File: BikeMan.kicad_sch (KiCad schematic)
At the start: 10 parts, among them J1 USB_A_stacked, J2 USB_A_stacked, J3 Conn_01x04_Female, J4 Barrel_Jack, J5 PushConnector_8pos, J6 PushConnector_8pos, J7 PushConnector_8pos

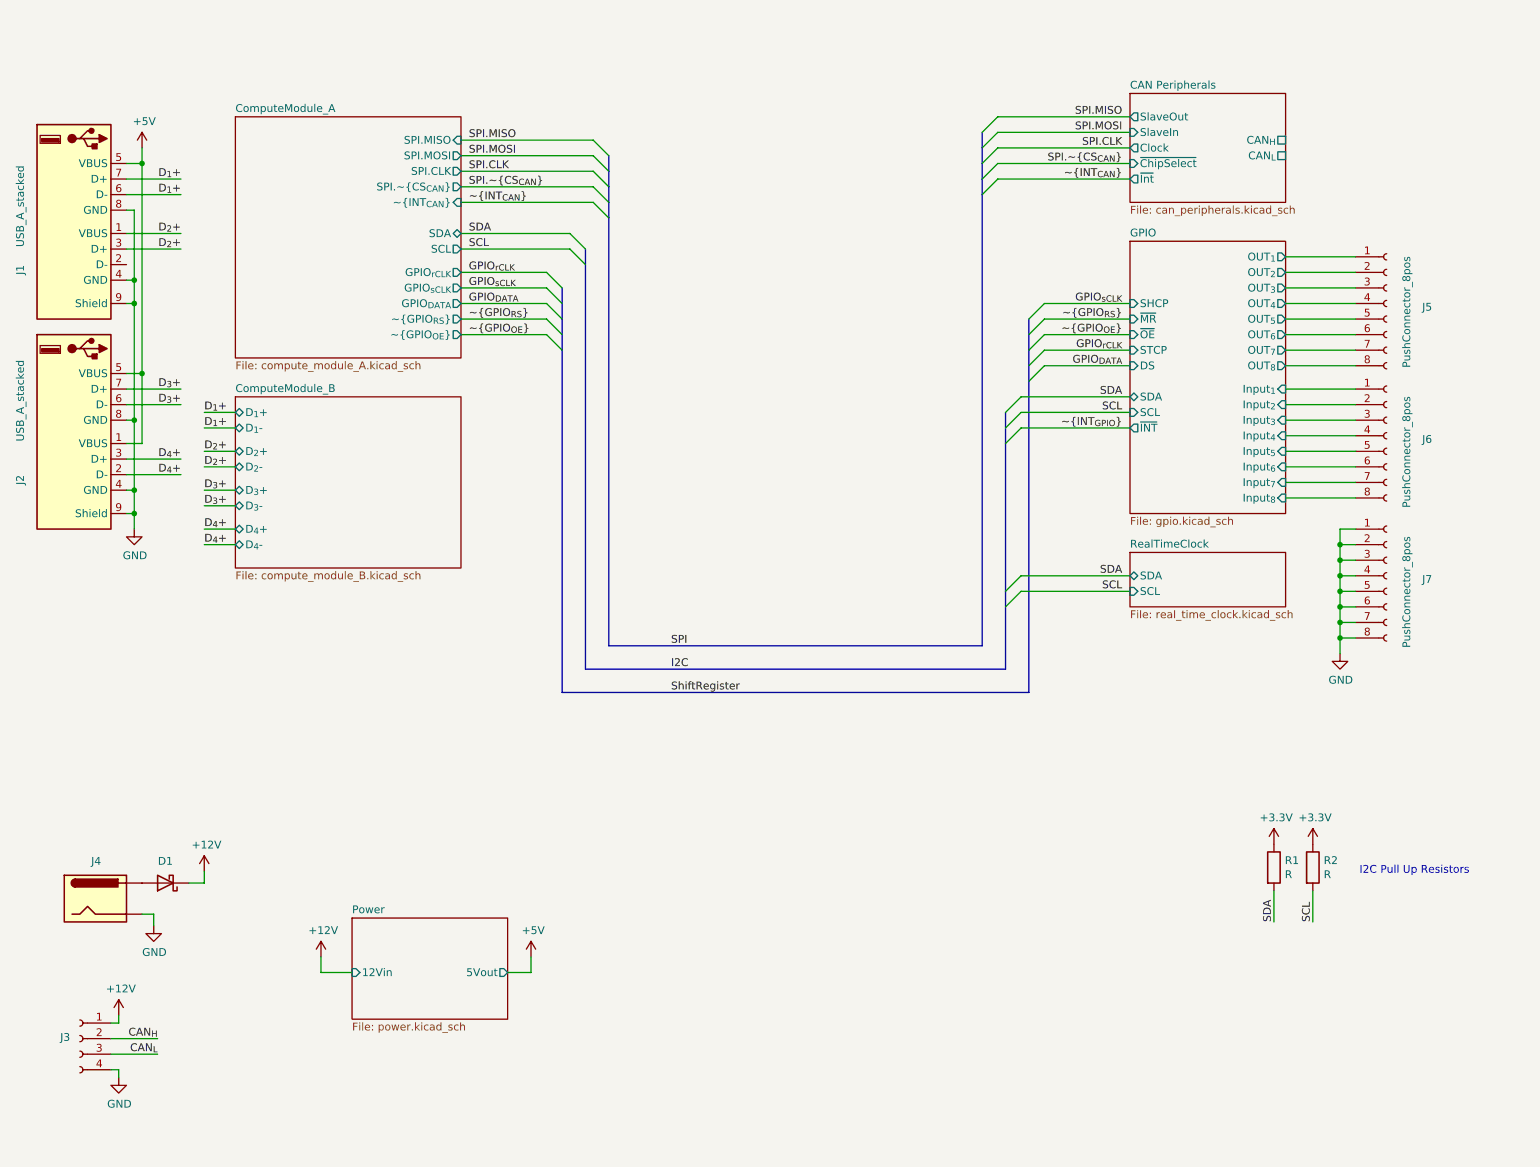
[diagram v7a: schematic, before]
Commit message: Added Daughter Card
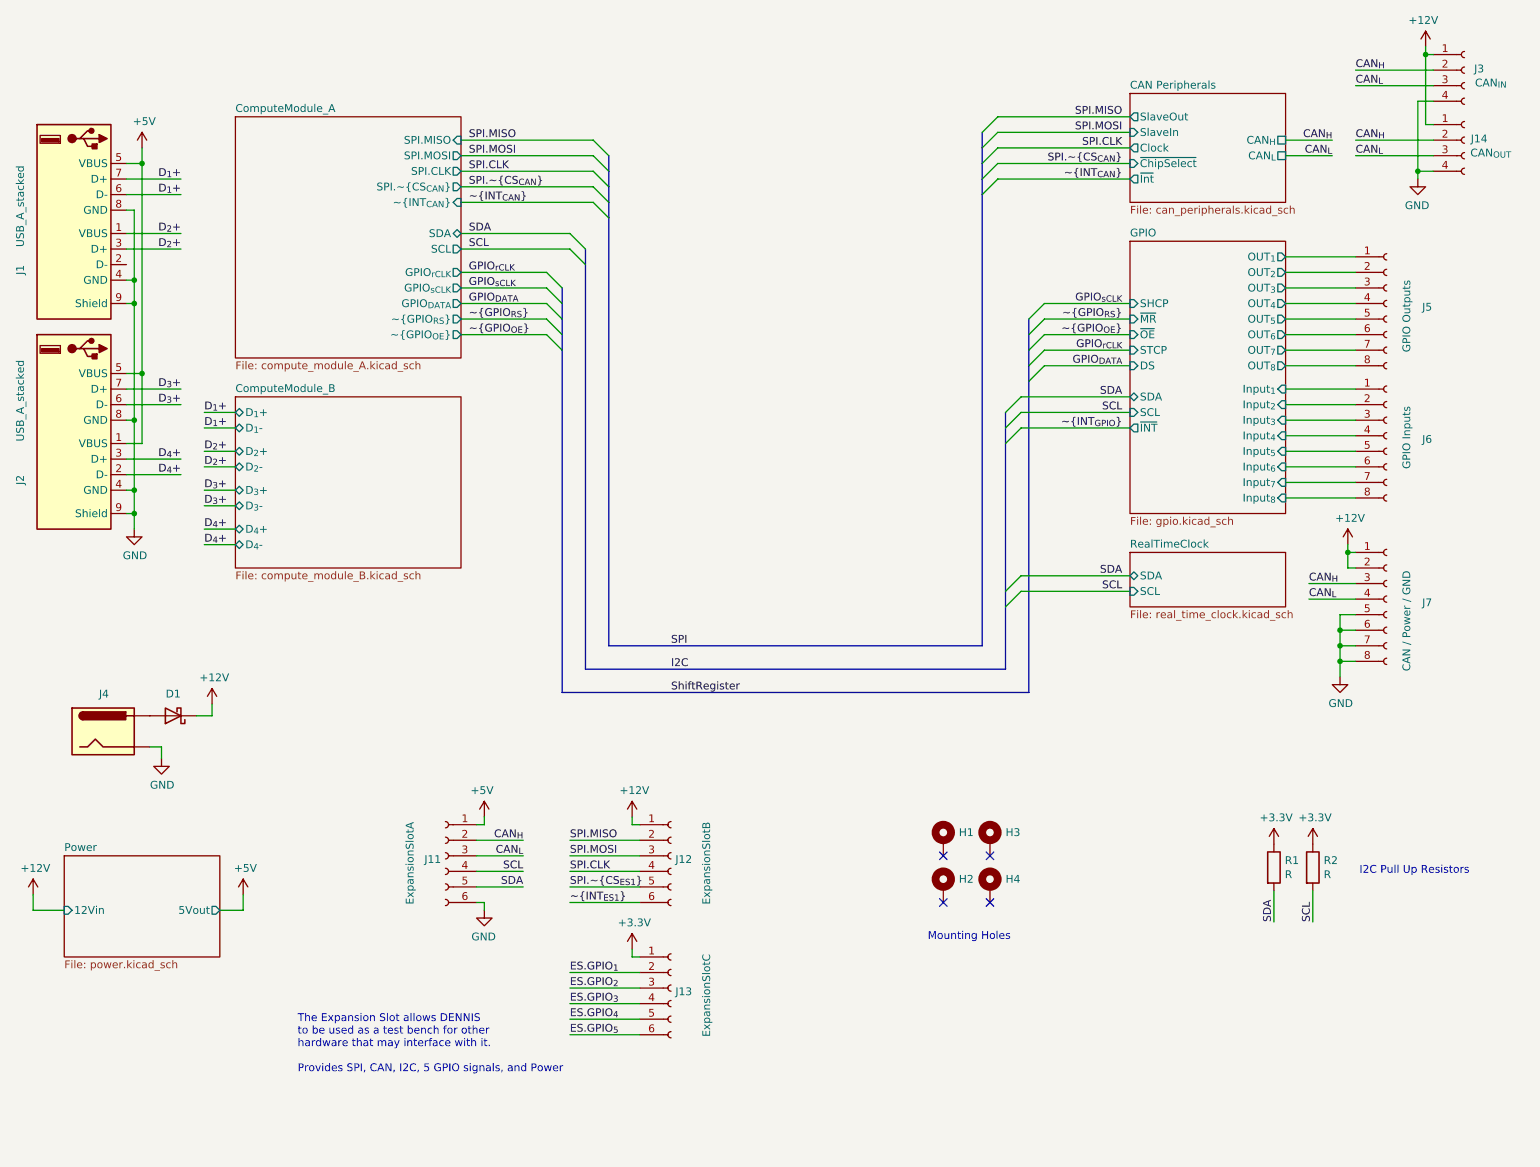
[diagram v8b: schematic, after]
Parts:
- added H1, H2, H3, H4: MountingHole_Pad, MountingHole:MountingHole_3.2mm_M3, symbol Mechanical:MountingHole_Pad
- added J11: ExpansionSlotA, Connector_PinSocket_2.54mm:PinSocket_2x03_P2.54mm_Vertical, symbol Connector:Conn_01x06_Female
- added J12: ExpansionSlotB, Connector_PinSocket_2.54mm:PinSocket_2x03_P2.54mm_Vertical, symbol Connector:Conn_01x06_Female
- added J13: ExpansionSlotC, Connector_PinSocket_2.54mm:PinSocket_2x03_P2.54mm_Vertical, symbol Connector:Conn_01x06_Female
- added J14: CAN_{OUT}, Connector_Molex:Molex_Micro-Fit_3.0_43045-0412_2x02_P3.00mm_Vertical, symbol Connector:Conn_01x04_Female
- J3: value Conn_01x04_Female -> CAN_{IN}; footprint (none) -> Connector_Molex:Molex_Micro-Fit_3.0_43045-0412_2x02_P3.00mm_Vertical
- J5: value PushConnector_8pos -> GPIO Outputs
- J6: value PushConnector_8pos -> GPIO Inputs
- J7: value PushConnector_8pos -> CAN / Power / GND
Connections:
- net +12V: now also J7.1 (Pin_1), J7.2 (Pin_2), J12.1 (Pin_1), J14.1 (Pin_1)
- net +3V3: now also J13.1 (Pin_1)
- net +5V: now also J11.1 (Pin_1)
- net CAN_{H}: now also J7.3 (Pin_3), J11.2 (Pin_2), J14.2 (Pin_2)
- net CAN_{L}: now also J7.4 (Pin_4), J11.3 (Pin_3), J14.3 (Pin_3)
- net GND: now also J11.6 (Pin_6), J14.4 (Pin_4); no longer J7.1 (Pin_1), J7.2 (Pin_2), J7.3 (Pin_3), J7.4 (Pin_4)
- net SCL: now also J11.4 (Pin_4)
- net SDA: now also J11.5 (Pin_5)
- net SPI.CLK: now also J12.4 (Pin_4)
- net SPI.MISO: now also J12.2 (Pin_2)
- net SPI.MOSI: now also J12.3 (Pin_3)
- new net ES.GPIO_{1}: J13.2 (Pin_2)
- new net ES.GPIO_{2}: J13.3 (Pin_3)
- new net ES.GPIO_{3}: J13.4 (Pin_4)
- new net ES.GPIO_{4}: J13.5 (Pin_5)
- new net ES.GPIO_{5}: J13.6 (Pin_6)
- new net SPI.~CS_{ES1}: J12.5 (Pin_5)
- new net ~INT_{ES1}: J12.6 (Pin_6)
- no-connect marks 0 -> 4
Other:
- note added: "Mounting Holes"
- note added: "The Expansion Slot allows DENNIS to be used as a test bench for other hardware that may interface with it. Provides SPI, CAN, I2C, 5 GPIO signals, and Power"
- moved on the sheet: D1, J3, J4, J7
